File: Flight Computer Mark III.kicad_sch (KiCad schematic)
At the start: 69 parts, among them J1 Conn_01x02, J2 USB_C_Receptacle_USB2.0_16P, Q1 PSMN075-100MSE, Q2 PSMN075-100MSE, Q3 PSMN075-100MSE, U1 CP2102N-Axx-xQFN20

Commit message: lol
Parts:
- removed CLK1, MISO1, MOSI1: SolderJumper_2_Open, Capacitor_SMD:C_0603_1608Metric, symbol Jumper:SolderJumper_2_Open
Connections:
- net CLK_SPIEXT is gone; now on net CLK_SPI0: SPI_EXT1.6 (Pin_6)
- net MISO_SPIEXT is gone; now on net MISO_SPI0: SPI_EXT1.4 (Pin_4)
- net MOSI_SPIEXT is gone; now on net MOSI_SPI0: SPI_EXT1.3 (Pin_3)
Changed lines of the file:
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@@
 	(global_label "CLK_SPIEXT"
 		(shape output)
-		(at 273.05 60.96 0)
+		(at 265.43 60.96 0)
 		(effects
 			(font
@@
 		)
 		(property "Intersheetrefs" "${INTERSHEET_REFS}"
-			(at 273.05 60.96 0)
+			(at 265.43 60.96 0)
 			(effects
 				(font
@@
 	(global_label "MOSI_SPIEXT"
 		(shape output)
-		(at 273.05 76.2 0)
+		(at 265.43 76.2 0)
 		(effects
 			(font
@@
 		)
 		(property "Intersheetrefs" "${INTERSHEET_REFS}"
-			(at 273.05 76.2 0)
+			(at 265.43 76.2 0)
 			(effects
 				(font
@@
 	(global_label "MISO_SPIEXT"
 		(shape input)
-		(at 273.05 68.58 0)
+		(at 265.43 68.58 0)
 		(effects
 			(font
@@
 		)
 		(property "Intersheetrefs" "${INTERSHEET_REFS}"
-			(at 273.05 68.58 0)
+			(at 265.43 68.58 0)
 			(effects
 				(font
@@
 	)
 	(symbol
-		(lib_id "Jumper:SolderJumper_2_Open")
-		(at 269.24 60.96 0)
-		(unit 1)
-		(exclude_from_sim yes)
-		(in_bom no)
-		(on_board yes)
-		(dnp no)
-		(property "Reference" "CLK1"
-			(at 268.986 58.674 0)
-			(effects
-				(font
-					(size 1.27 1.27)
-				)
-			)
-		)
-		(property "Value" "SolderJumper_2_Open"
-			(at 268.986 58.42 0)
-			(effects
-				(font
-					(size 1.27 1.27)
-				)
-				(hide yes)
-			)
-		)
-		(property "Footprint" "Capacitor_SMD:C_0603_1608Metric"
-			(at 269.24 60.96 0)
-			(effects
-				(font
-					(size 1.27 1.27)
-				)
-				(hide yes)
-			)
-		)
-		(property "Datasheet" "~"
-			(at 269.24 60.96 0)
-			(effects
-				(font
-					(size 1.27 1.27)
-				)
-				(hide yes)
-			)
-		)
-		(property "Description" "Solder Jumper, 2-pole, open"
-			(at 269.24 60.96 0)
-			(effects
-				(font
-					(size 1.27 1.27)
-				)
-				(hide yes)
-			)
-		)
-		(pin "2"
-		)
-		(pin "1"
-		)
-		(instances
-			(project "Flight Computer Mark III"
-				(path "/0bad6c6f-d77b-4b1f-bd5d-3c971ec5e274"
-					(reference "CLK1")
-					(unit 1)
-				)
-			)
-		)
-	)
-	(symbol
 		(lib_id "Flight Computer:Pyro-Pad")
 		(at 167.64 193.04 90)
@@
 	)
 	(symbol
-		(lib_id "Jumper:SolderJumper_2_Open")
-		(at 269.24 76.2 0)
-		(unit 1)
-		(exclude_from_sim yes)
-		(in_bom no)
-		(on_board yes)
-		(dnp no)
-		(property "Reference" "MOSI1"
-			(at 268.986 78.486 0)
-			(effects
-				(font
-					(size 1.27 1.27)
-				)
-			)
-		)
-		(property "Value" "SolderJumper_2_Open"
-			(at 268.986 73.66 0)
-			(effects
-				(font
-					(size 1.27 1.27)
-				)
-				(hide yes)
-			)
-		)
-		(property "Footprint" "Capacitor_SMD:C_0603_1608Metric"
-			(at 269.24 76.2 0)
-			(effects
-				(font
-					(size 1.27 1.27)
-				)
-				(hide yes)
-			)
-		)
-		(property "Datasheet" "~"
-			(at 269.24 76.2 0)
-			(effects
-				(font
-					(size 1.27 1.27)
-				)
-				(hide yes)
-			)
-		)
-		(property "Description" "Solder Jumper, 2-pole, open"
-			(at 269.24 76.2 0)
-			(effects
-				(font
-					(size 1.27 1.27)
-				)
-				(hide yes)
-			)
-		)
-		(pin "2"
-		)
-		(pin "1"
-		)
-		(instances
-			(project ""
-				(path "/0bad6c6f-d77b-4b1f-bd5d-3c971ec5e274"
-					(reference "MOSI1")
-					(unit 1)
-				)
-			)
-		)
-	)
-	(symbol
 		(lib_name "CGA0402X5R226M100GT_1_1")
 		(lib_id "CGA0402X5R226M100GT_1")
@@
 					(unit 1)
 				)
-			)
-		)
-	)
-	(symbol
-		(lib_id "Jumper:SolderJumper_2_Open")
-		(at 269.24 68.58 0)
-		(unit 1)
-		(exclude_from_sim yes)
-		(in_bom no)
-		(on_board yes)
-		(dnp no)
-		(property "Reference" "MISO1"
-			(at 268.986 70.866 0)
-			(effects
-				(font
-					(size 1.27 1.27)
-				)
-			)
-		)
-		(property "Value" "SolderJumper_2_Open"
-			(at 268.986 66.04 0)
-			(effects
-				(font
-					(size 1.27 1.27)
-				)
-				(hide yes)
-			)
-		)
-		(property "Footprint" "Capacitor_SMD:C_0603_1608Metric"
-			(at 269.24 68.58 0)
-			(effects
-				(font
-					(size 1.27 1.27)
-				)
-				(hide yes)
-			)
-		)
-		(property "Datasheet" "~"
-			(at 269.24 68.58 0)
-			(effects
-				(font
-					(size 1.27 1.27)
-				)
-				(hide yes)
-			)
-		)
-		(property "Description" "Solder Jumper, 2-pole, open"
-			(at 269.24 68.58 0)
-			(effects
-				(font
-					(size 1.27 1.27)
-				)
-				(hide yes)
-			)
-		)
-		(pin "2"
-		)
-		(pin "1"
-		)
-		(instances
-			(project "Flight Computer Mark III"
-				(path "/0bad6c6f-d77b-4b1f-bd5d-3c971ec5e274"
-					(reference "MISO1")
-					(unit 1)
-				)

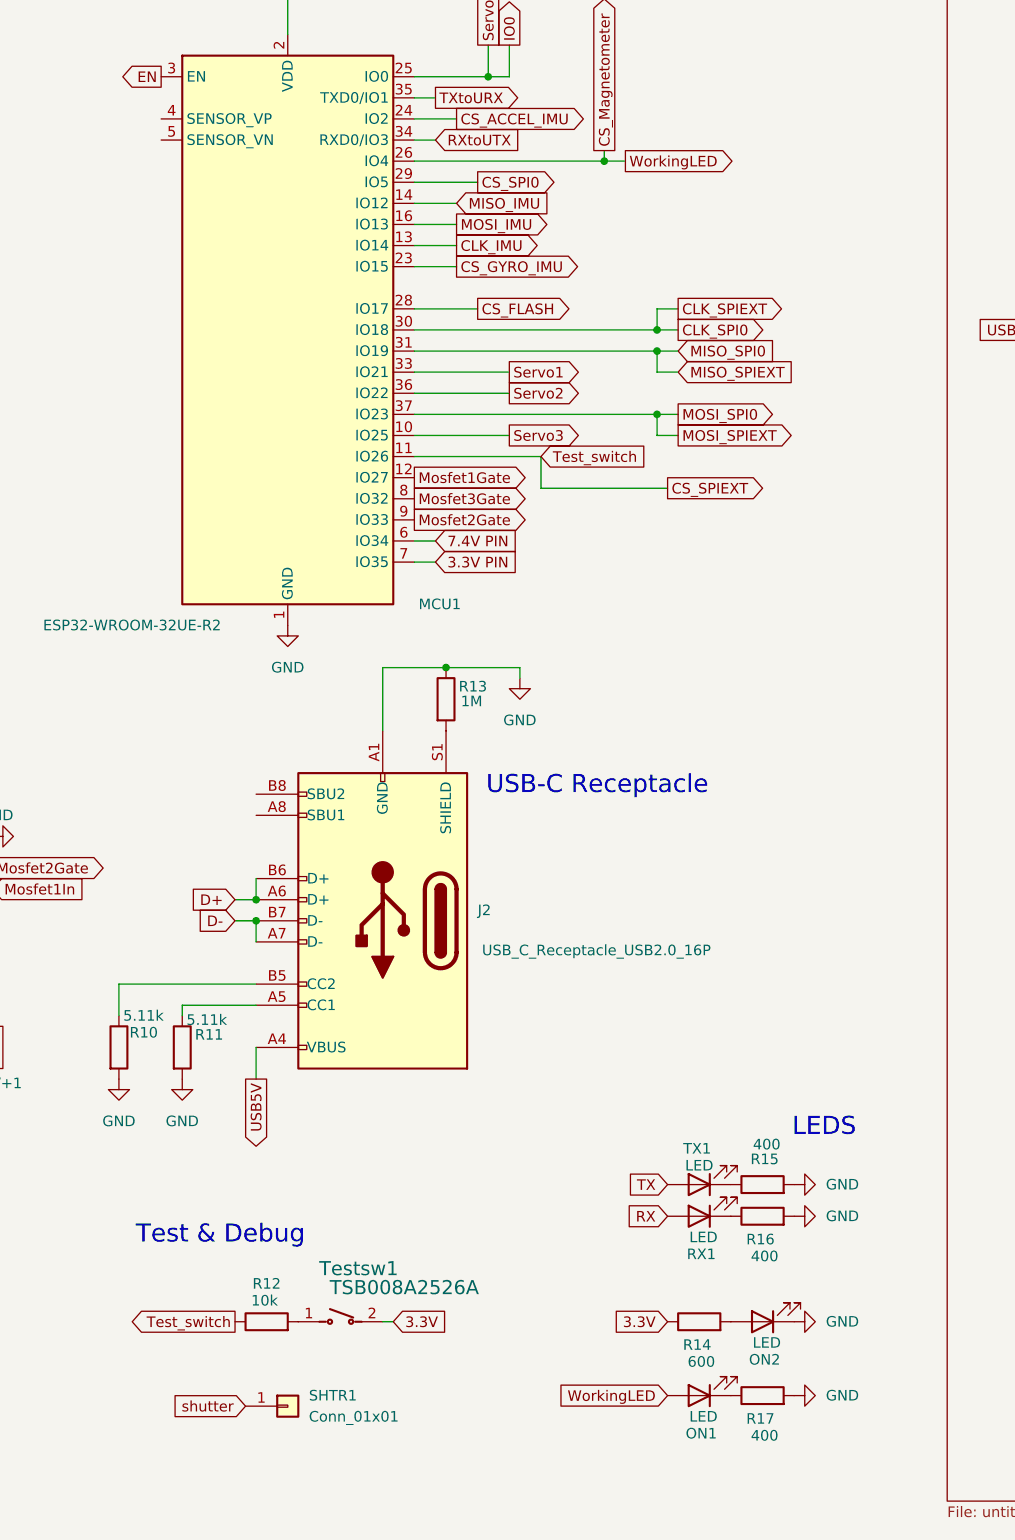
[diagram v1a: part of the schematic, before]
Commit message: Changed some via diameters, added 3D models, restructured the GND planes
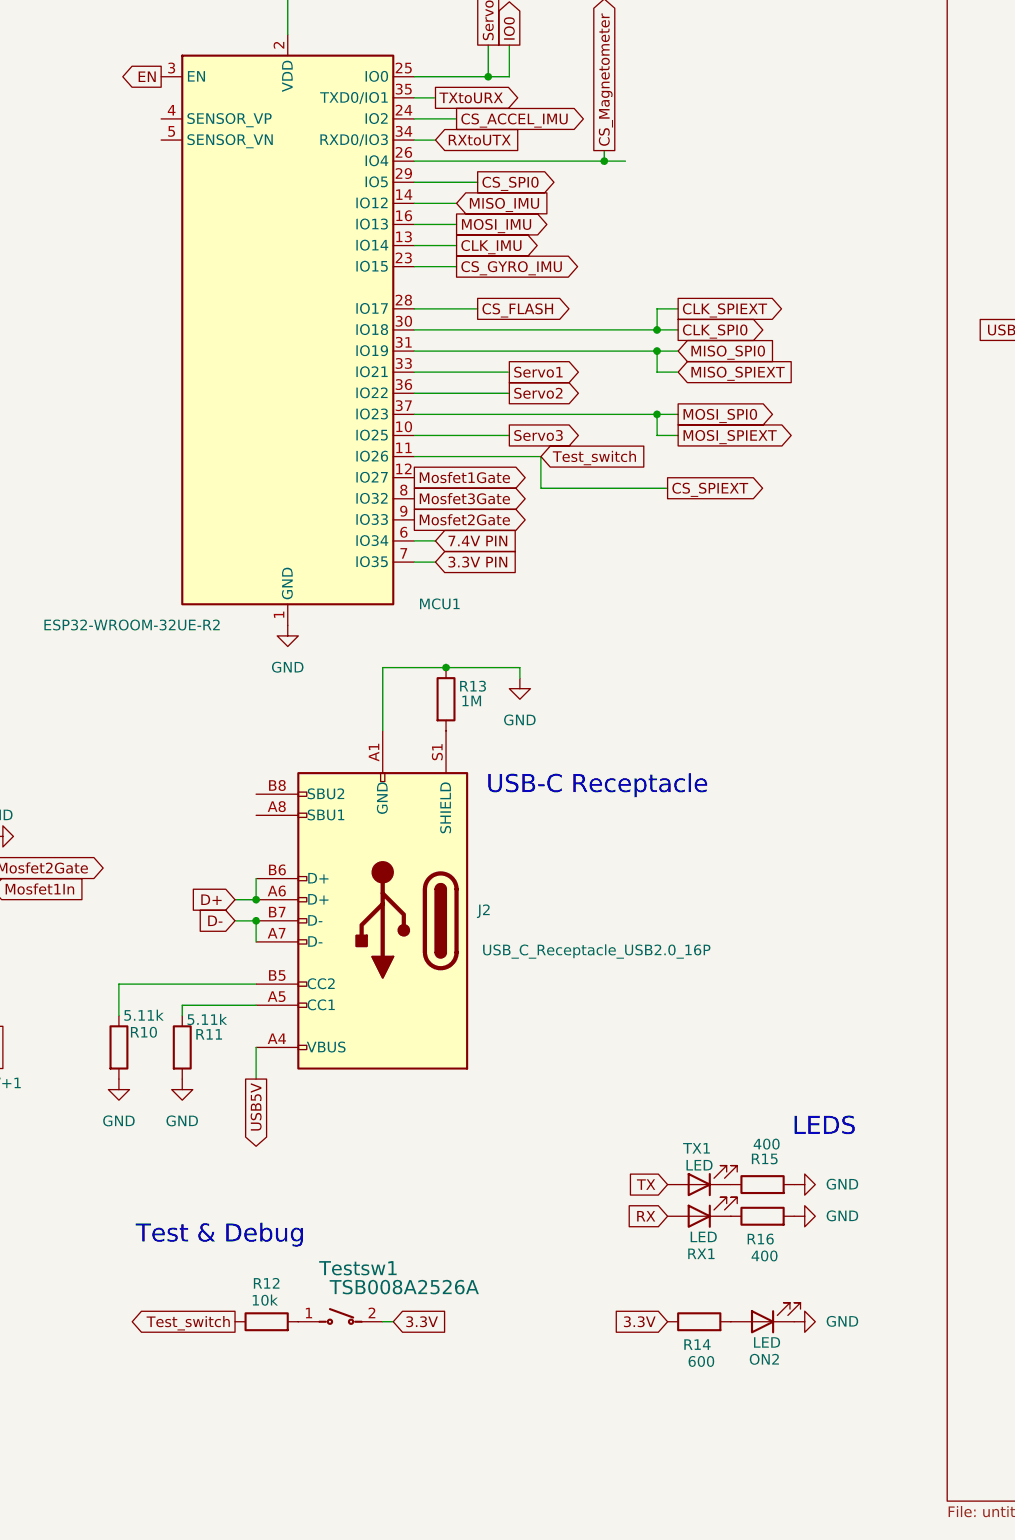
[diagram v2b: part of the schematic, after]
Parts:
- removed ON1: LED, LED_SMD:LED_0805_2012Metric, symbol Device:LED
- removed R17: 400, Resistor_SMD:R_0603_1608Metric, symbol Device:R
- removed SHTR1: Conn_01x01, Connector_PinHeader_2.54mm:PinHeader_1x01_P2.54mm_Vertical, symbol Connector_Generic:Conn_01x01
